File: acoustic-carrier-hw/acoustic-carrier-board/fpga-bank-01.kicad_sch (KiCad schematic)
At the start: 11 parts, among them IC1 ECP5-BGA256, Y401 Crystal Oscillator

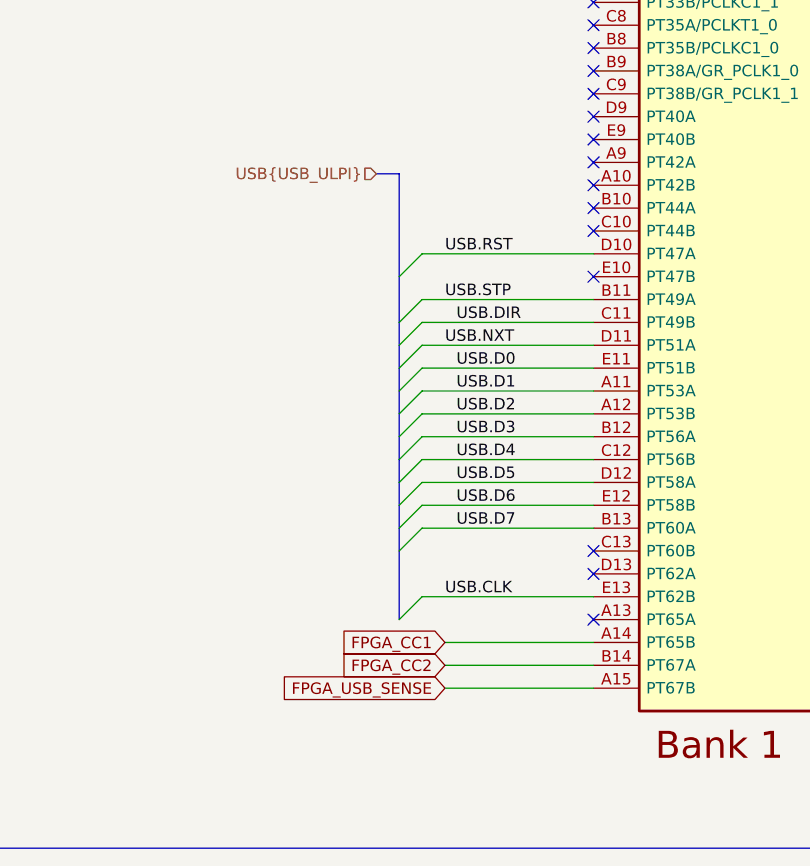
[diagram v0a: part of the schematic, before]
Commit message: [carrier] Routing out RGMII interface
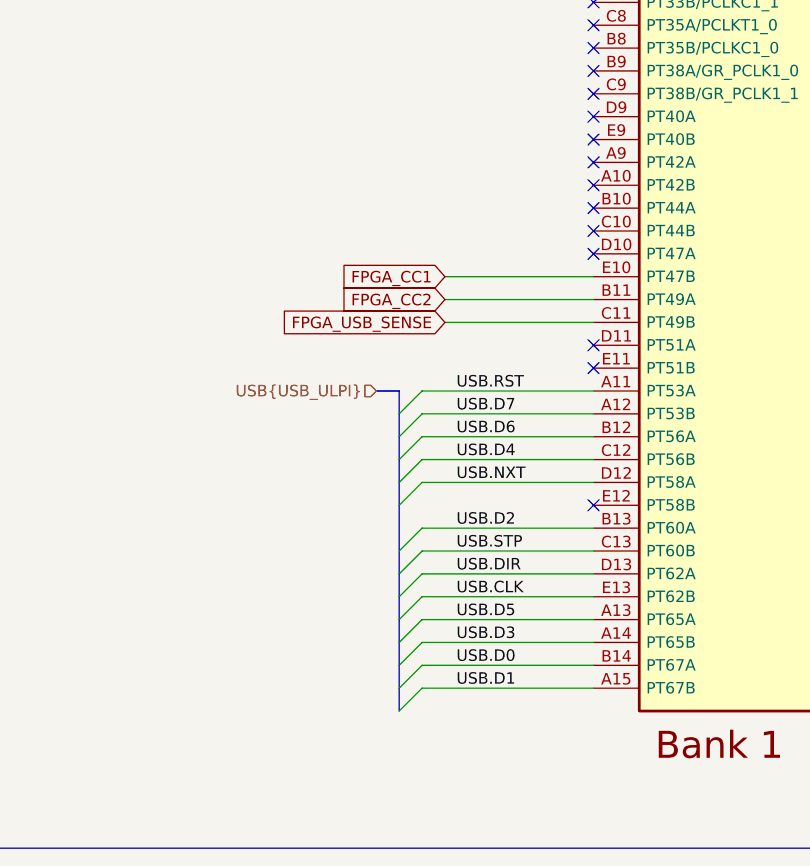
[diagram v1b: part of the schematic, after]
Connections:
- net FPGA_CC1: now also IC1.E10 (PT47B); no longer IC1.A14 (PT65B)
- net FPGA_CC2: now also IC1.B11 (PT49A); no longer IC1.B14 (PT67A)
- net FPGA_USB_SENSE: now also IC1.C11 (PT49B); no longer IC1.A15 (PT67B)
- net USB.D0: now also IC1.B14 (PT67A); no longer IC1.E11 (PT51B)
- net USB.D1: now also IC1.A15 (PT67B); no longer IC1.A11 (PT53A)
- net USB.D2: now also IC1.B13 (PT60A); no longer IC1.A12 (PT53B)
- net USB.D3: now also IC1.A14 (PT65B); no longer IC1.B12 (PT56A)
- net USB.D5: now also IC1.A13 (PT65A); no longer IC1.D12 (PT58A)
- net USB.D6: now also IC1.B12 (PT56A); no longer IC1.E12 (PT58B)
- net USB.D7: now also IC1.A12 (PT53B); no longer IC1.B13 (PT60A)
- net USB.DIR: now also IC1.D13 (PT62A); no longer IC1.C11 (PT49B)
- net USB.NXT: now also IC1.D12 (PT58A); no longer IC1.D11 (PT51A)
- net USB.RST: now also IC1.A11 (PT53A); no longer IC1.D10 (PT47A)
- net USB.STP: now also IC1.C13 (PT60B); no longer IC1.B11 (PT49A)

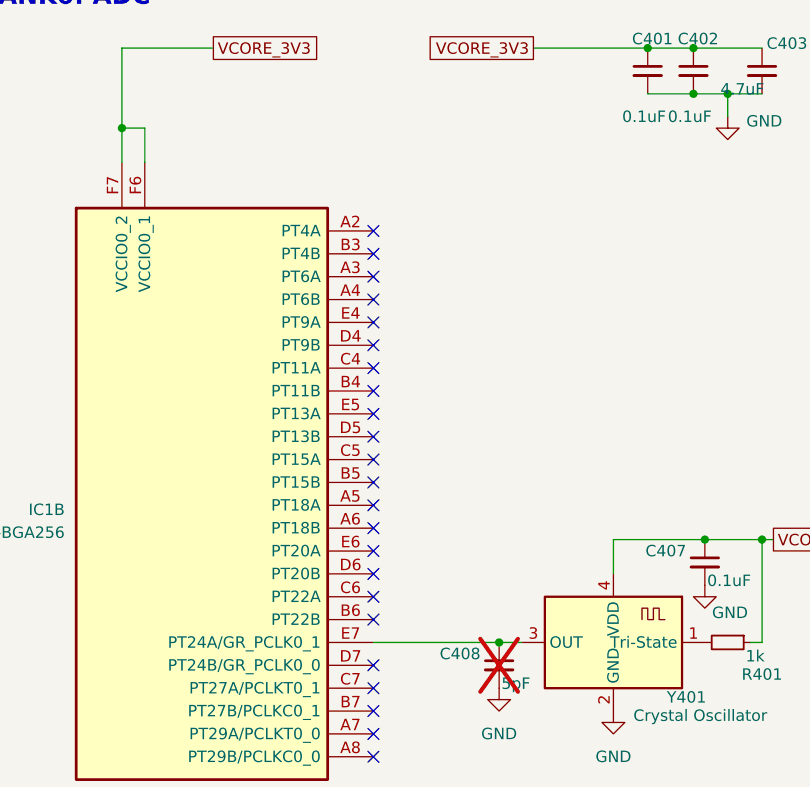
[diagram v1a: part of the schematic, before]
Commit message: [carrier] Routed out signals for board-to-board PTH
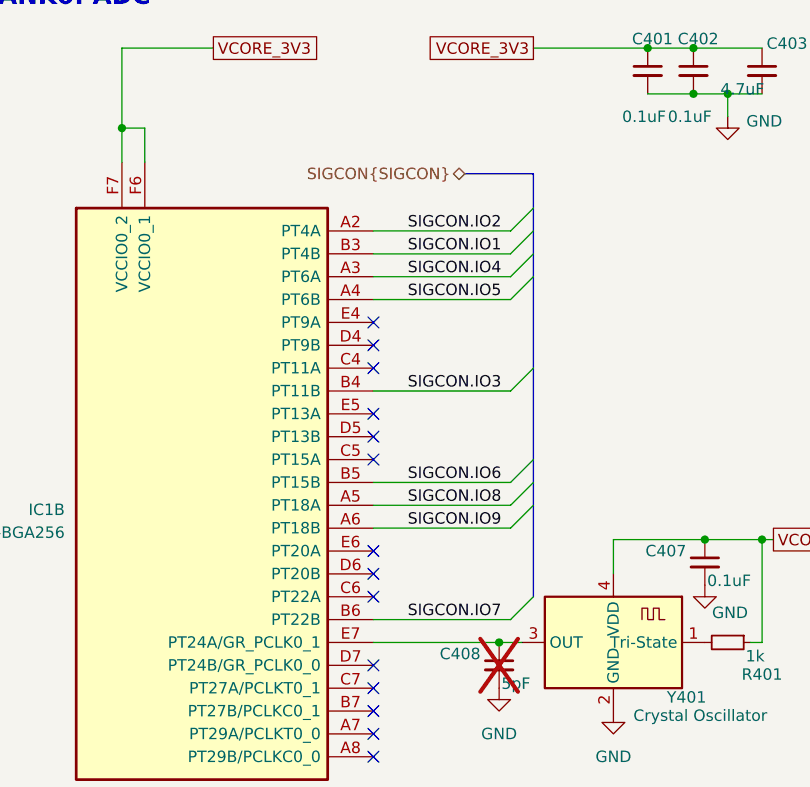
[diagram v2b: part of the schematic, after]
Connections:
- net SIGCON.IO2: now reaches IC1.A2 (PT4A)
- net SIGCON.IO4: now reaches IC1.A3 (PT6A)
- net SIGCON.IO5: now reaches IC1.A4 (PT6B)
- net SIGCON.IO8: now reaches IC1.A5 (PT18A)
- net SIGCON.IO9: now reaches IC1.A6 (PT18B)
- net SIGCON.IO1: now reaches IC1.B3 (PT4B)
- net SIGCON.IO3: now reaches IC1.B4 (PT11B)
- net SIGCON.IO6: now reaches IC1.B5 (PT15B)
- net SIGCON.IO7: now reaches IC1.B6 (PT22B)
- no-connect marks 39 -> 30

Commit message: [carrier] Changed all vias to (pcheaper) 0.2/0.35 size (next) create basic test-VHDL for clock-signal fanout checks
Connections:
- net FPGA_USB_SENSE: no longer names the net of IC1.C11 (PT49B)
- no-connect marks 30 -> 31
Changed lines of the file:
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@@
+	)
+	(no_connect
+		(at 237.49 97.79)
 	)
 	(no_connect
@@
 		(pts
 			(xy 100.33 72.39) (xy 100.33 82.55)
-		)
-		(stroke
-			(width 0)
-			(type default)
-		)
-	)
-	(wire
-		(pts
-			(xy 237.49 97.79) (xy 220.98 97.79)
 		)
 		(stroke
@@
 				(hide yes)
 			)
-		)
-	)
-	(global_label "FPGA_USB_SENSE"
-		(shape input)
-		(at 220.98 97.79 180)
-		(fields_autoplaced yes)
-		(effects
-			(font
-				(size 1.27 1.27)
-			)
-			(justify right)
-		)
-		(property "Intersheetrefs" "${INTERSHEET_REFS}"
-			(at 201.4849 97.79 0)
-			(effects
-				(font
-					(size 1.27 1.27)
-				)
-				(justify right)
-				(hide yes)
-			)

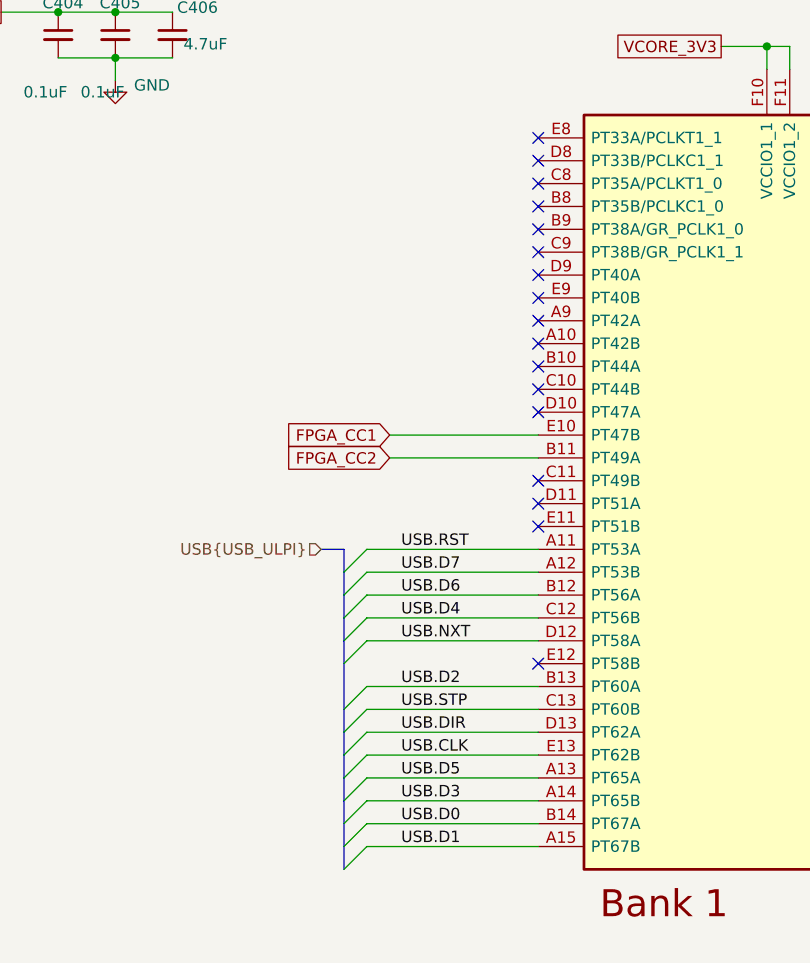
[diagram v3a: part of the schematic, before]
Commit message: [carrier] Rerouted USB-clock, checked setupp and hold conditions, length-matched ULPI
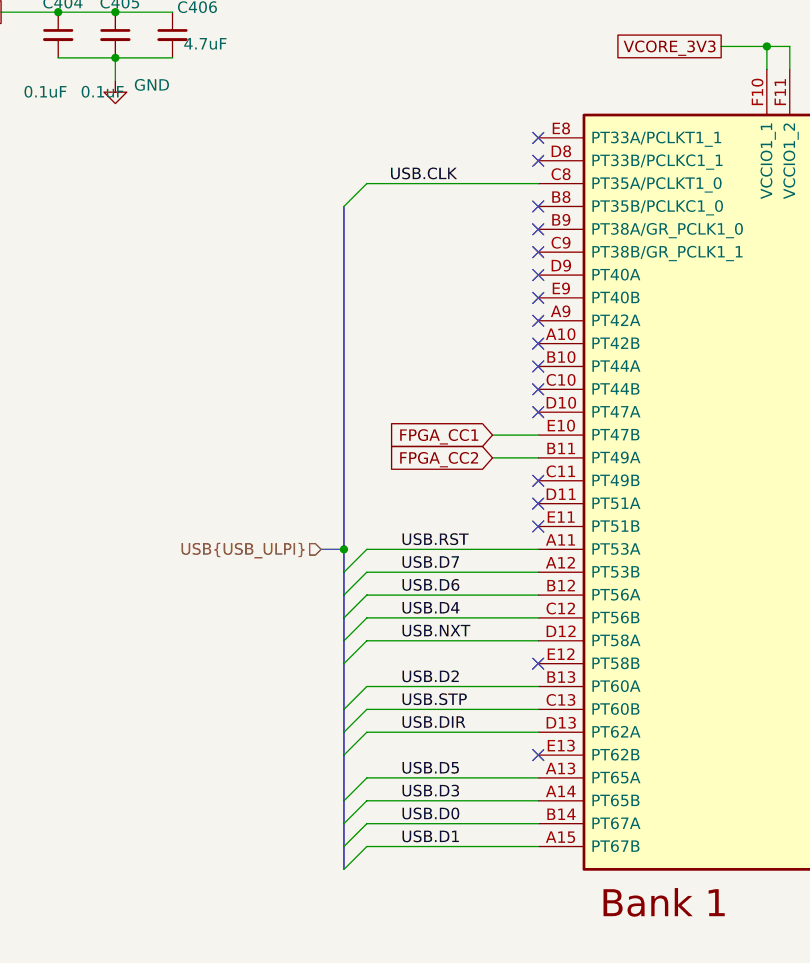
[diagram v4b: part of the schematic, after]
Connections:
- net USB.CLK: now also IC1.C8 (PT35A/PCLKT1_0); no longer IC1.E13 (PT62B)
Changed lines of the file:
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@@
+	)
+	(junction
+		(at 215.9 105.41)
+		(diameter 0)
+		(color 0 0 0 0)
 	)
 	(junction
@@
 	)
 	(no_connect
+		(at 237.49 128.27)
+	)
+	(no_connect
 		(at 237.49 80.01)
 	)
@@
 	(no_connect
 		(at 82.55 123.19)
-	)
-	(no_connect
-		(at 237.49 64.77)
 	)
 	(no_connect
@@
 	)
 	(bus_entry
+		(at 215.9 67.31)
+		(size 2.54 -2.54)
+		(stroke
+			(width 0)
+			(type default)
+		)
+	)
+	(bus_entry
 		(at 97.79 74.93)
 		(size 2.54 -2.54)
@@
 	)
 	(bus_entry
-		(at 218.44 128.27)
-		(size -2.54 2.54)
-		(stroke
-			(width 0)
-			(type default)
-		)
-	)
-	(bus_entry
 		(at 97.79 110.49)
 		(size 2.54 -2.54)
@@
 		)
 	)
+	(bus
+		(pts
+			(xy 215.9 67.31) (xy 215.9 105.41)
+		)
+		(stroke
+			(width 0)
+			(type default)
+		)
+	)
 	(wire
 		(pts
@@
 	(wire
 		(pts
+			(xy 218.44 64.77) (xy 237.49 64.77)
+		)
+		(stroke
+			(width 0)
+			(type default)
+		)
+	)
+	(wire
+		(pts
 			(xy 82.55 113.03) (xy 96.52 113.03)
 		)
@@
 	(wire
 		(pts
-			(xy 237.49 92.71) (xy 220.98 92.71)
+			(xy 237.49 92.71) (xy 232.41 92.71)
 		)
 		(stroke
@@
 		)
 	)
-	(bus
-		(pts
-			(xy 215.9 130.81) (xy 215.9 133.35)
-		)
-		(stroke
-			(width 0)
-			(type default)
-		)
-	)
 	(wire
 		(pts
@@
 		)
 	)
-	(wire
-		(pts
-			(xy 237.49 128.27) (xy 218.44 128.27)
-		)
-		(stroke
-			(width 0)
-			(type default)
-		)
-	)
 	(bus
 		(pts
@@
 	(bus
 		(pts
-			(xy 215.9 128.27) (xy 215.9 130.81)
-		)
-		(stroke
-			(width 0)
-			(type default)
-		)
-	)
-	(wire
-		(pts
-			(xy 237.49 95.25) (xy 220.98 95.25)
+			(xy 215.9 128.27) (xy 215.9 133.35)
+		)
+		(stroke
+			(width 0)
+			(type default)
+		)
+	)
+	(wire
+		(pts
+			(xy 237.49 95.25) (xy 232.41 95.25)
 		)
 		(stroke
@@
 		)
 	)
+	(label "USB.CLK"
+		(at 220.98 64.77 0)
+		(effects
+			(font
+				(size 1.27 1.27)
+			)
+			(justify left bottom)
+		)
+	)
 	(label "SIGCON.IO2"
 		(at 86.36 67.31 0)
@@
 		)
 	)
-	(label "USB.CLK"
-		(at 222.25 128.27 0)
-		(effects
-			(font
-				(size 1.27 1.27)
-			)
-			(justify left bottom)
-		)
-	)
 	(label "USB.DIR"
 		(at 222.25 125.73 0)
@@
 	(global_label "FPGA_CC2"
 		(shape input)
-		(at 220.98 95.25 180)
+		(at 232.41 95.25 180)
 		(fields_autoplaced yes)
 		(effects
@@
 		)
 		(property "Intersheetrefs" "${INTERSHEET_REFS}"
-			(at 208.5605 95.25 0)
+			(at 219.9905 95.25 0)
 			(effects
 				(font
@@
 	(global_label "FPGA_CC1"
 		(shape input)
-		(at 220.98 92.71 180)
+		(at 232.41 92.71 180)
 		(fields_autoplaced yes)
 		(effects
@@
 		)
 		(property "Intersheetrefs" "${INTERSHEET_REFS}"
-			(at 208.5605 92.71 0)
+			(at 219.9905 92.71 0)
 			(effects
 				(font

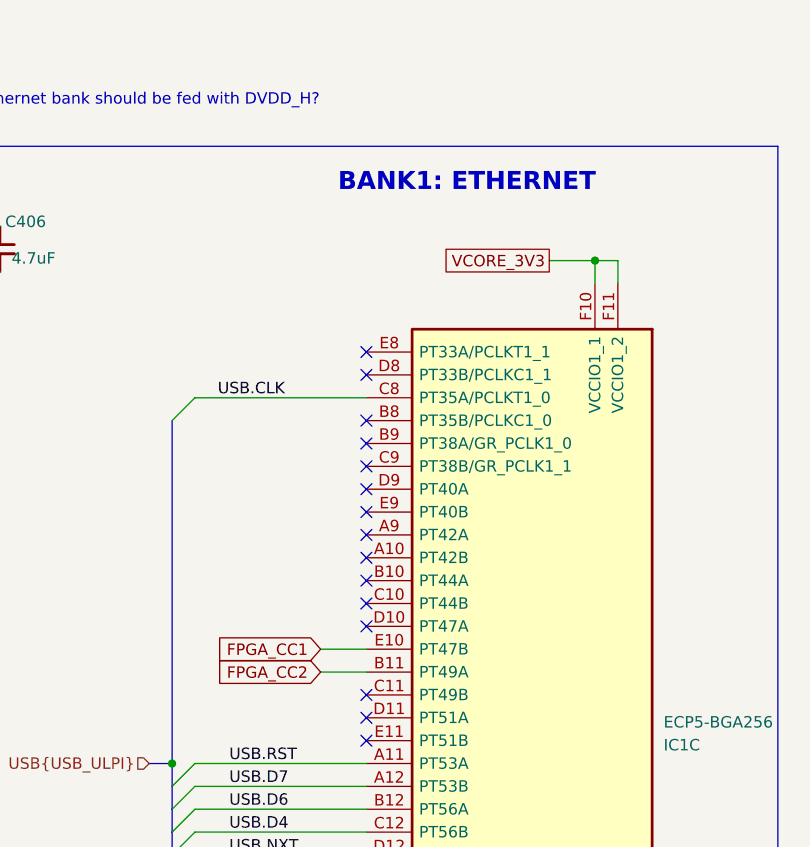
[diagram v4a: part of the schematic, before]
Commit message: [carrier] Started writing constraints file for ECP5U-FPGA (next) finish constraints file, try basic synthesis with pins and hello-world
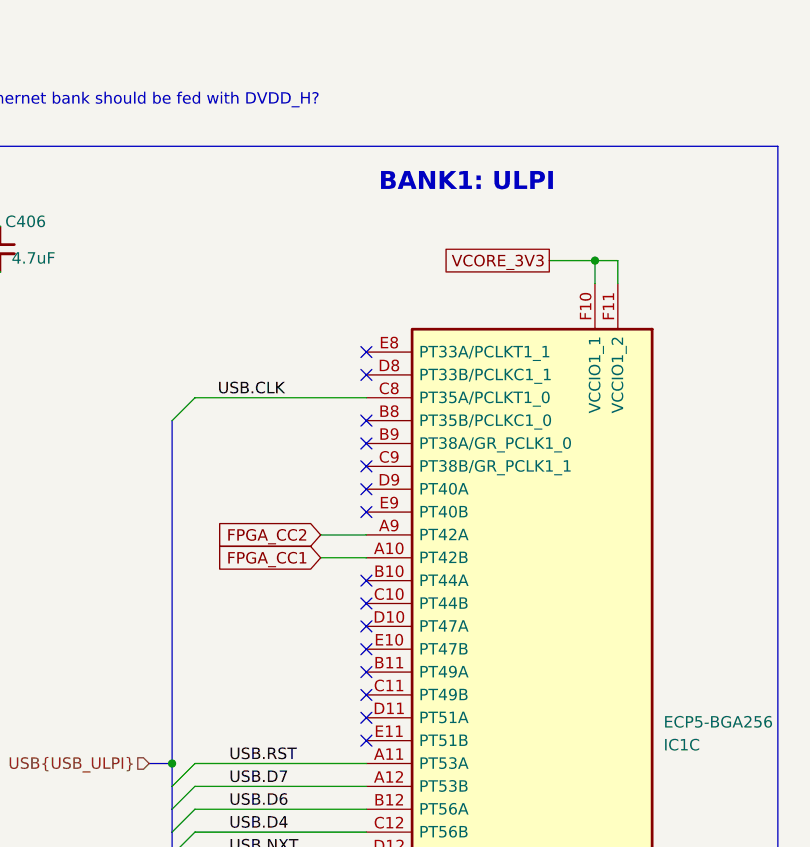
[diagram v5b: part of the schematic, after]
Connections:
- net FPGA_CC1: now also IC1.A10 (PT42B); no longer IC1.E10 (PT47B)
- net FPGA_CC2: now also IC1.A9 (PT42A); no longer IC1.B11 (PT49A)
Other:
- note added: "BANK1: ULPI"
- note removed: "BANK1: ETHERNET"
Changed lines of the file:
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@@
 		)
 	)
-	(text "BANK1: ETHERNET"
+	(text "BANK1: ULPI\n"
 		(exclude_from_sim no)
 		(at 248.666 40.894 0)
@@
 	)
 	(no_connect
-		(at 237.49 82.55)
-	)
-	(no_connect
 		(at 237.49 59.69)
 	)
@@
 	)
 	(no_connect
+		(at 237.49 95.25)
+	)
+	(no_connect
 		(at 237.49 87.63)
 	)
@@
 	)
 	(no_connect
-		(at 237.49 80.01)
-	)
-	(no_connect
 		(at 237.49 90.17)
 	)
@@
 	(no_connect
 		(at 237.49 118.11)
+	)
+	(no_connect
+		(at 237.49 92.71)
 	)
 	(no_connect
@@
 	(wire
 		(pts
-			(xy 237.49 92.71) (xy 232.41 92.71)
-		)
-		(stroke
-			(width 0)
-			(type default)
-		)
-	)
-	(wire
-		(pts
 			(xy 237.49 113.03) (xy 218.44 113.03)
 		)
@@
 	(wire
 		(pts
+			(xy 237.49 80.01) (xy 232.41 80.01)
+		)
+		(stroke
+			(width 0)
+			(type default)
+		)
+	)
+	(wire
+		(pts
 			(xy 218.44 115.57) (xy 237.49 115.57)
 		)
@@
 	(wire
 		(pts
+			(xy 237.49 82.55) (xy 232.41 82.55)
+		)
+		(stroke
+			(width 0)
+			(type default)
+		)
+	)
+	(wire
+		(pts
 			(xy 190.5 50.8) (xy 196.85 50.8)
 		)
@@
 		(pts
 			(xy 215.9 128.27) (xy 215.9 133.35)
-		)
-		(stroke
-			(width 0)
-			(type default)
-		)
-	)
-	(wire
-		(pts
-			(xy 237.49 95.25) (xy 232.41 95.25)
 		)
 		(stroke
@@
 			)
 			(justify left bottom)
-		)
-	)
-	(global_label "FPGA_CC2"
-		(shape input)
-		(at 232.41 95.25 180)
-		(fields_autoplaced yes)
-		(effects
-			(font
-				(size 1.27 1.27)
-			)
-			(justify right)
-		)
-		(property "Intersheetrefs" "${INTERSHEET_REFS}"
-			(at 219.9905 95.25 0)
-			(effects
-				(font
-					(size 1.27 1.27)
-				)
-				(justify right)
-				(hide yes)
-			)
 		)
 	)
@@
 	(global_label "FPGA_CC1"
 		(shape input)
-		(at 232.41 92.71 180)
+		(at 232.41 82.55 180)
 		(fields_autoplaced yes)
 		(effects
@@
 		)
 		(property "Intersheetrefs" "${INTERSHEET_REFS}"
-			(at 219.9905 92.71 0)
+			(at 219.9905 82.55 0)
 			(effects
 				(font
+					(size 1.27 1.27)
+				)
+				(justify right)
+				(hide yes)
+			)
+		)
+	)
+	(global_label "FPGA_CC2"
+		(shape input)
+		(at 232.41 80.01 180)
+		(fields_autoplaced yes)
+		(effects
+			(font
+				(size 1.27 1.27)
+			)
+			(justify right)
+		)
+		(property "Intersheetrefs" "${INTERSHEET_REFS}"
+			(at 219.9905 80.01 0)
+			(effects
+				(font
